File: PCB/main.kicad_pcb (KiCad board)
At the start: 2 copper layers, 64 parts, among them J1 S20B-PADSS-1, J2 S20B-PADSS-1, J3 SWD, SW1 SPST, U1 TPS5430, U2 AMS1117-3.3, U3 MCP2558FD, U4 MCP2558FD, U5 STM32G0B1, Y1 40M

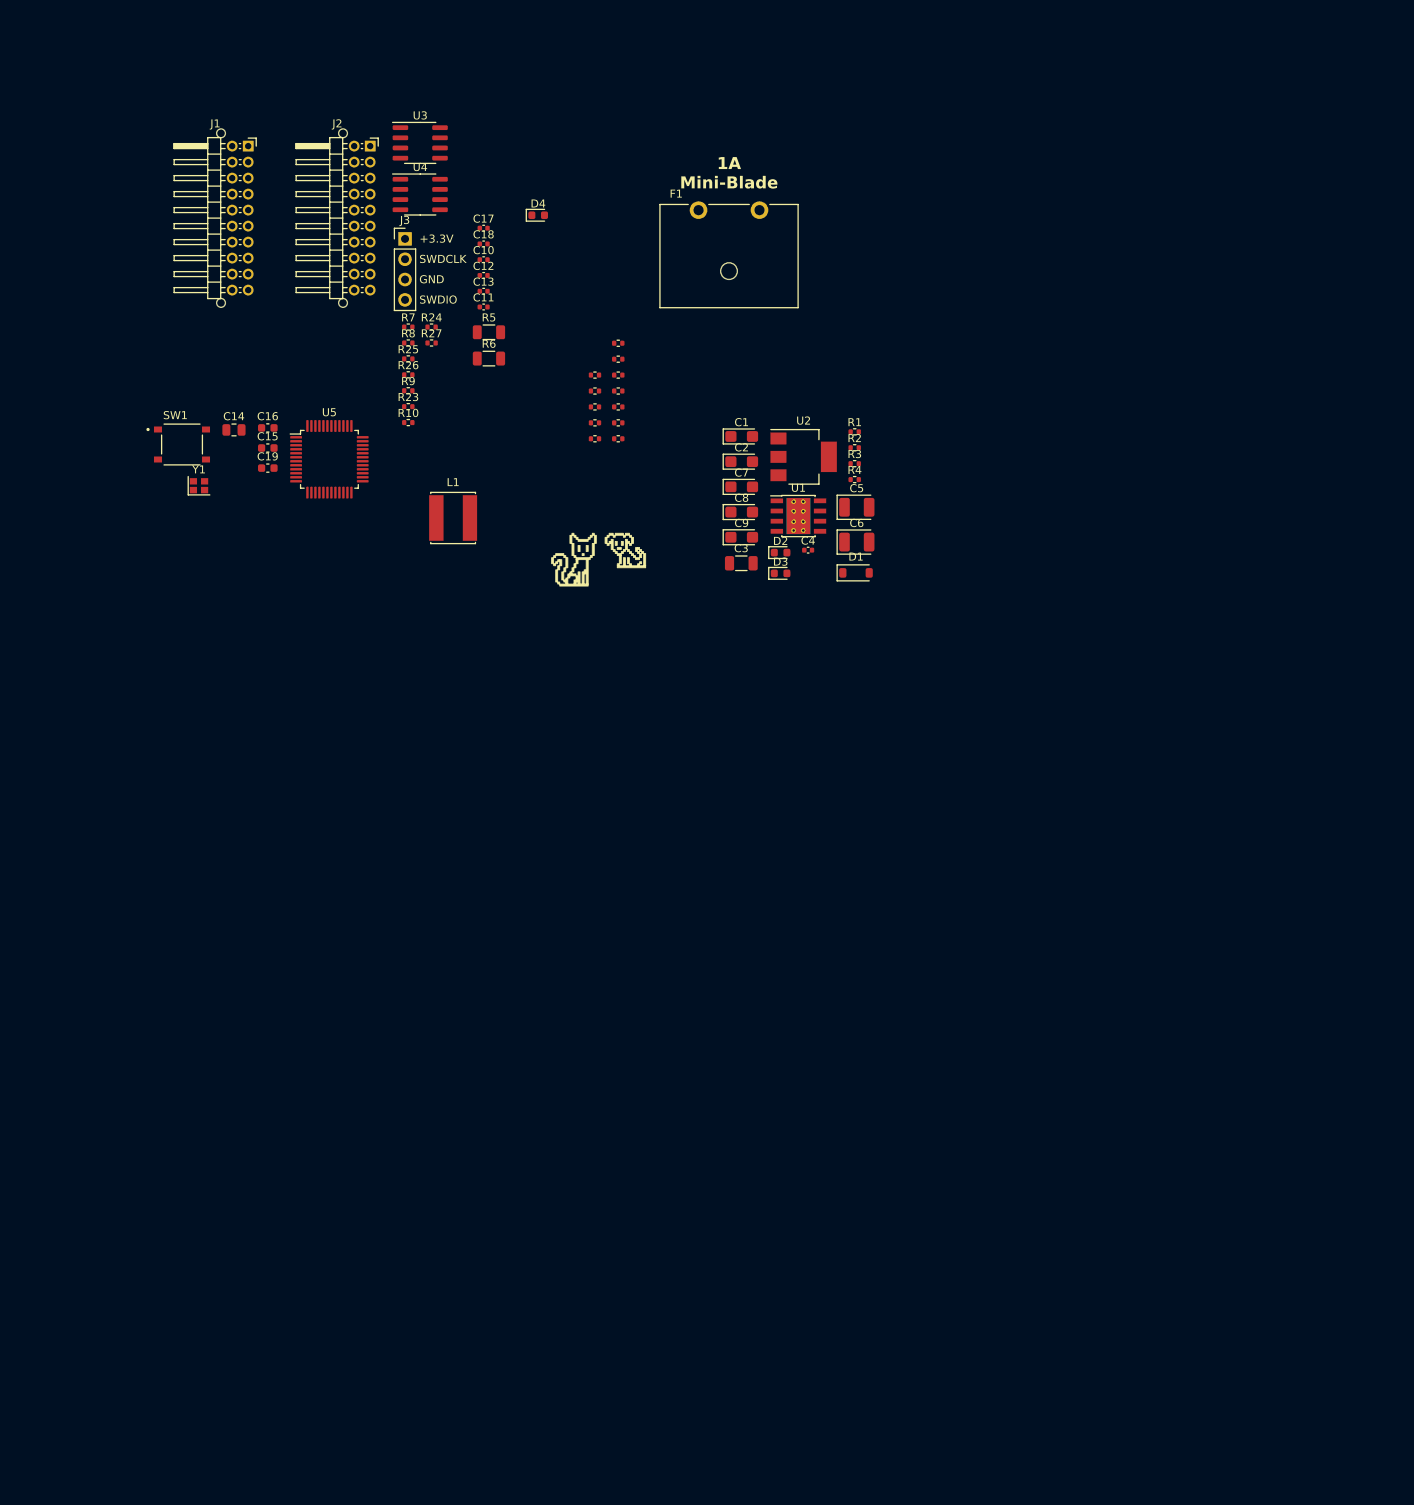
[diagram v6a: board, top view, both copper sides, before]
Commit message: Start layout, but intend to ditch the 0ohm resistors and be confident CAN1 is the right one (remember 0402 links)
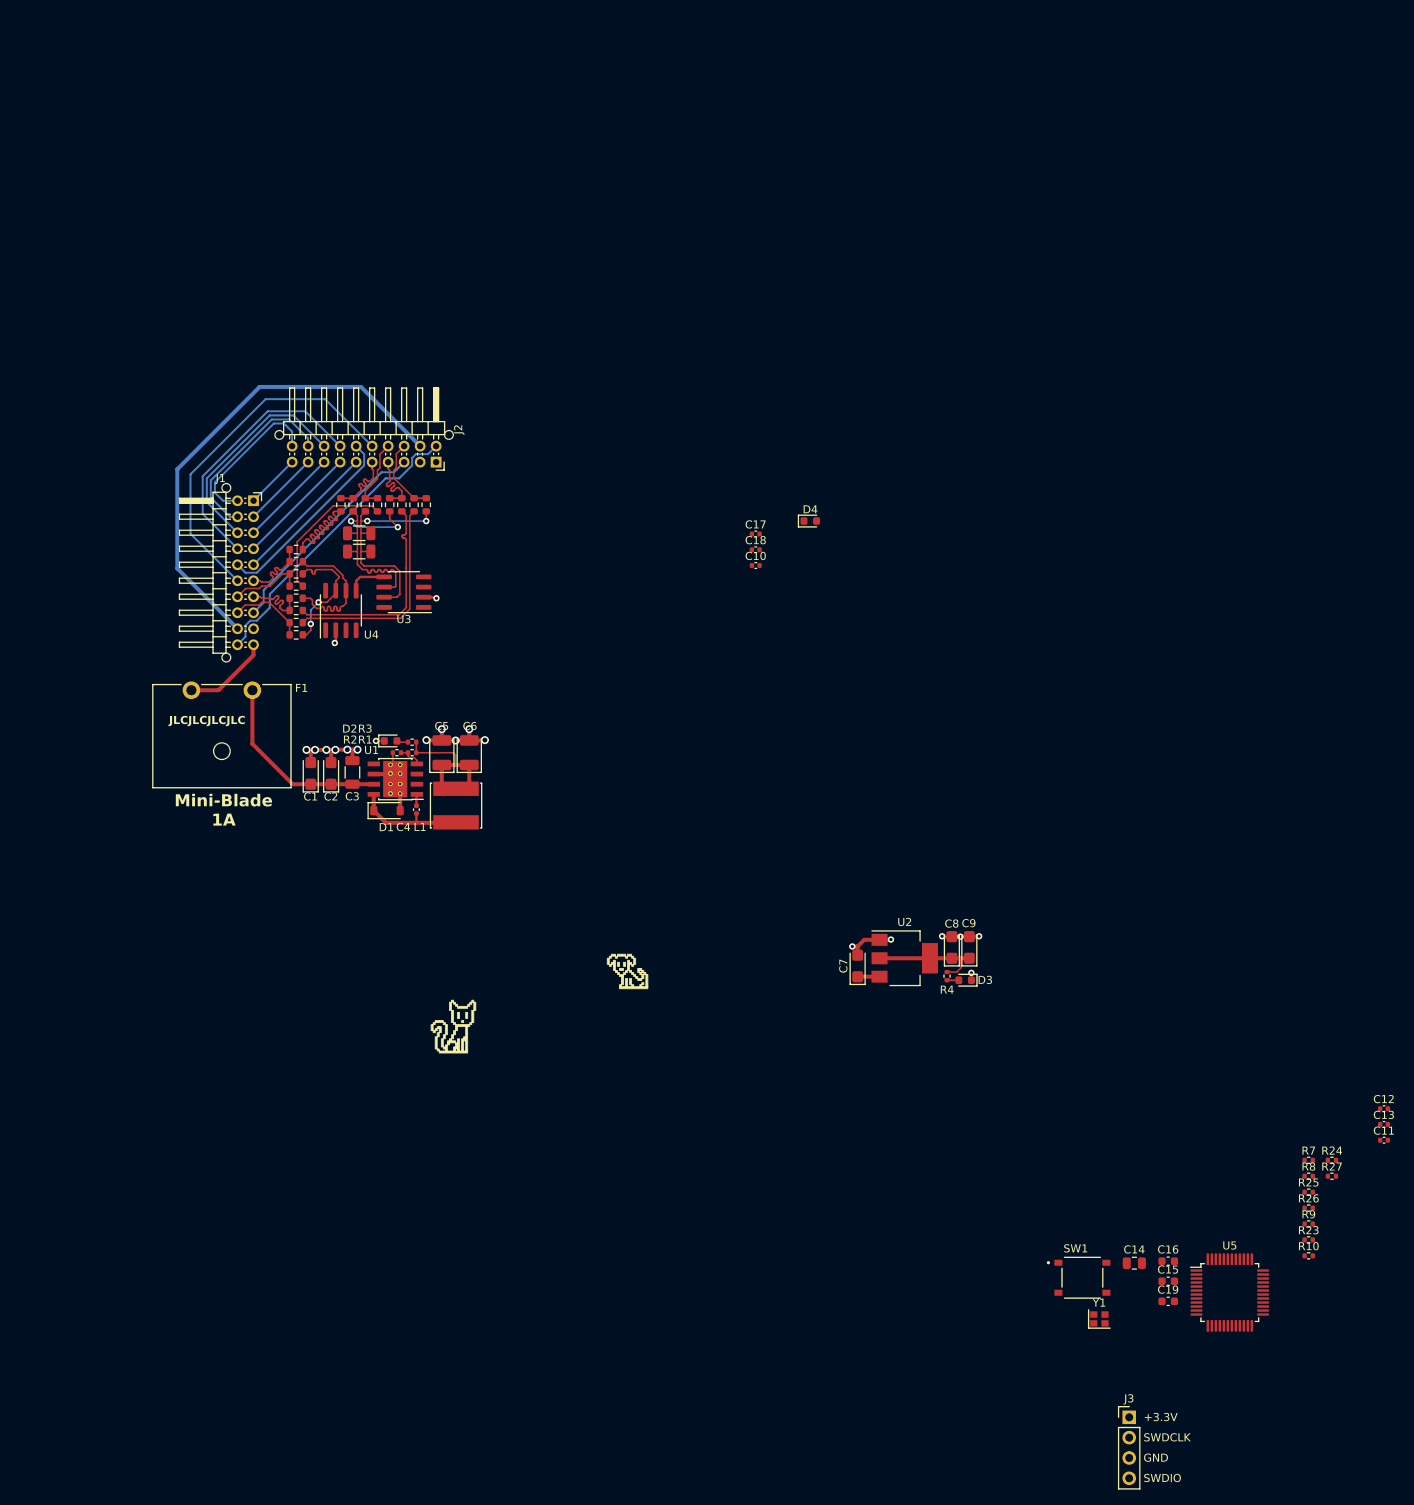
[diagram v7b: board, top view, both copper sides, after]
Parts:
- added ART3: JLCJLCJLCJLC, libdb:CMP-0047, F.Cu at (28.7, 90.0)
- added R28: 0, Resistor_SMD:R_0603_1608Metric, F.Cu at (47.5, 64.8)
- added R29: 0, Resistor_SMD:R_0603_1608Metric, F.Cu at (42.9, 64.8)
- added R30: 0, Resistor_SMD:R_0603_1608Metric, F.Cu at (52.1, 64.8)
- added R31: 0, Resistor_SMD:R_0603_1608Metric, F.Cu at (50.5, 64.8)
- R11, R12, R13, R14, R15, R16, R17, R18, R19, R20, R21, R22: footprint Resistor_SMD:R_0402_1005Metric -> Resistor_SMD:R_0603_1608Metric
- moved J3 172.9 mm to (141.5, 178.8)
- moved C15 153.3 mm to (146.3, 161.8)
- moved C16 153.3 mm to (146.3, 159.3)
- moved C19 153.3 mm to (146.3, 164.3)
- moved R10 153.3 mm to (163.9, 158.6)
- moved R24 153.3 mm to (166.8, 146.7)
- moved R26 153.3 mm to (163.9, 152.7)
- moved R27 153.3 mm to (166.8, 148.7)
- moved R7 153.3 mm to (163.9, 146.7)
- moved R8 153.3 mm to (163.9, 148.7)
- moved R9 153.3 mm to (163.9, 154.7)
- moved SW1 153.3 mm to (135.6, 161.4)
- moved Y1 153.3 mm to (137.7, 166.5)
- moved C11 153.3 mm to (173.3, 144.2)
- moved C12 153.3 mm to (173.3, 140.3)
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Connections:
- net /JST_06_CAN1L renamed /IN_CAN1-
- net /JST_07_CAN2L_NC renamed /IN_NC_CAN2-
- net /JST_17_CAN1H renamed /IN_CAN1+
- net /JST_18_CAN2H_NC renamed /IN_NC_CAN2+
- net /Relay_IN_CANH renamed /Relay_IN_CAN+
- net /Relay_IN_CANL renamed /Relay_IN_CAN-
- net /Relay_OUT_CANH renamed /Relay_OUT_CAN+
- net /Relay_OUT_CANL renamed /Relay_OUT_CAN-
- F1 pad 1: +BATT -> /JST_10_BAT+
- F1 pad 2: /JST_10_BAT+ -> +BATT
- J2 pad 13: /CAN2H_NC -> /NC_CAN2+
- J2 pad 14: /CAN1H -> /CAN1+
- J2 pad 4: /CAN2L_NC -> /NC_CAN2-
- J2 pad 5: /CAN1L -> /CAN1-
- R15 pad 1: /CAN1H -> /CAN1+
- R16 pad 1: /CAN2H_NC -> /NC_CAN2+
- R17 pad 1: /CAN1H -> /CAN1-
- R18 pad 1: /CAN2H_NC -> /NC_CAN2-
- R19 pad 1: /CAN1H -> /FW_CAN1+
- R20 pad 1: /CAN1L -> /FW_CAN1-
- R21 pad 1: /CAN2H_NC -> /FW_NC_CAN2+
- R22 pad 1: /CAN2L_NC -> /FW_NC_CAN2-
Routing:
- net /JST_19_CAM_12V+: track 0.00 -> 60.7 mm
- net /JST_10_BAT+: track 0.00 -> 50.9 mm
- net /JST_16_NC: track 0.00 -> 44.8 mm
- net Earth: track 0.00 -> 42.8 mm, vias 0 -> 20
- net /JST_20_NC: track 0.00 -> 37.5 mm
- net /JST_14_AUDIO_FL: track 0.00 -> 33.2 mm
- net /Relay_OUT_CAN+: track 0.00 -> 28.8 mm, vias 0 -> 2
- net /Relay_OUT_CAN-: track 0.00 -> 28.6 mm, vias 0 -> 2
- net /JST_13_AUDIO_FL: track 0.00 -> 27.9 mm
- net /JST_08_CAM_DET: track 0.00 -> 27.5 mm
- net /FW_NC_CAN2+: track 0.00 -> 26.5 mm
- net /FW_NC_CAN2-: track 0.00 -> 26.5 mm
- net /JST_15_VID_IN: track 0.00 -> 24.6 mm
- net +BATT: track 0.00 -> 24.0 mm
- net /JST_12_AUDIO_FL: track 0.00 -> 23.7 mm
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- added copper zone on In1.Cu, net Earth
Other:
- copper layers 2 -> 4
- board text added: "Mini-Blade 1A"
- board text removed: "1A Mini-Blade"

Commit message: Start relayout
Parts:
- removed R28, R29, R30, R31: 0, Resistor_SMD:R_0603_1608Metric
- R11, R12, R13, R14, R15, R16, R17, R18, R19, R20, R21, R22: footprint Resistor_SMD:R_0603_1608Metric -> Resistor_SMD:R_0402_1005Metric
- U1: footprint Package_SO:TI_SO-PowerPAD-8_ThermalVias -> libdb:CMP-0030
- moved J3 142.3 mm to (105.0, 41.2)
- moved C11 136.1 mm to (71.7, 53.7), turned to -90 degrees
- moved U5 123.7 mm to (119.1, 44.6)
- moved Y1 119.7 mm to (126.7, 47.3)
- moved R23 115.1 mm to (117.8, 51.2)
- moved R10 112.7 mm to (114.9, 57.2)
- moved R9 110.9 mm to (114.9, 55.2)
- moved C15 108.7 mm to (111.3, 58.9)
- moved SW1 108.4 mm to (124.2, 53.6)
- moved R7 107.3 mm to (114.9, 51.2)
- moved R8 107.3 mm to (114.9, 53.2)
- moved C19 106.4 mm to (111.3, 63.9)
- moved R25 106.0 mm to (117.8, 55.2)
- moved R26 106.0 mm to (117.8, 57.2)
- moved R24 105.5 mm to (117.8, 53.2)
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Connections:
- net Earth renamed GND
- net Net-(D1-K) renamed /PH
- F1 pad 1: /JST_10_BAT+ -> +BATT
- F1 pad 2: +BATT -> /JST_10_BAT+
- R12 pad 1: /Relay_IN_CAN+ -> /NC_CAN2+
- R12 pad 2: /IN_NC_CAN2+ -> /FW_CAN2+
- R14 pad 1: /Relay_IN_CAN- -> /NC_CAN2-
- R14 pad 2: /IN_NC_CAN2- -> /FW_CAN2-
- R16 pad 1: /NC_CAN2+ -> /Relay_IN_CAN+
- R16 pad 2: /Relay_OUT_CAN+ -> /N2+
- R18 pad 1: /NC_CAN2- -> /Relay_IN_CAN-
- R18 pad 2: /Relay_OUT_CAN- -> /N2-
- R19 pad 1: /FW_CAN1+ -> /Relay_OUT_CAN+
- R19 pad 2: /IN_CAN1+ -> /N1+
- R20 pad 1: /FW_CAN1- -> /Relay_OUT_CAN-
- R20 pad 2: /IN_CAN1- -> /N1-
- R21 pad 1: /FW_NC_CAN2+ -> /FW_CAN2+
- R22 pad 1: /FW_NC_CAN2- -> /FW_CAN2-
- R5 pad 1: /Relay_OUT_CAN- -> /N1-
- R5 pad 2: /Relay_OUT_CAN+ -> /N1+
- R6 pad 1: /Relay_OUT_CAN- -> /N1-
- R6 pad 2: /Relay_OUT_CAN+ -> /N1+
- U3 pad 6: /Relay_OUT_CAN- -> /N1-
- U3 pad 7: /Relay_OUT_CAN+ -> /N1+
- U4 pad 6: /Relay_IN_CAN- -> /N2-
- U4 pad 7: /Relay_IN_CAN+ -> /N2+
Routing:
- net /JST_10_BAT+: track 50.9 -> 0.00 mm
- net /FW_CAN2-: track 0.00 -> 37.8 mm, vias 0 -> 2
- net /FW_CAN2+: track 0.00 -> 37.8 mm, vias 0 -> 2
- net /JST_01_AUX_IN: track 6.82 -> 44.6 mm
- net /JST_02_AUX_IN: track 9.65 -> 43.3 mm
- net GND: track 42.8 -> 9.86 mm, vias 20 -> 16
- net /JST_03_AUX_IN: track 12.5 -> 44.6 mm
- net /JST_11_AUDIO_FL: track 19.5 -> 48.8 mm
- net /JST_04_NC: track 15.3 -> 43.3 mm
- net /JST_12_AUDIO_FL: track 23.7 -> 51.4 mm
- net /Relay_OUT_CAN+: track 28.8 -> 1.30 mm, vias 2 -> 0
- net /Relay_OUT_CAN-: track 28.6 -> 1.30 mm, vias 2 -> 0
- net /FW_NC_CAN2+: track 26.5 -> 0.00 mm
- net /FW_NC_CAN2-: track 26.5 -> 0.00 mm
- net /JST_05_BK_VID_IN: track 18.1 -> 43.8 mm
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- added copper zone on F.Cu, net +3.3V
- added copper zone on F.Cu, net +5V
- added copper zone on F.Cu, net +BATT
- added copper zone on In2.Cu, net /JST_10_BAT+
- added copper zone on F.Cu, net /PH
- added copper zone on F.Cu, net GND
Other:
- board outline added: 115.2 x 62.3 mm
- board text added: "1A Mini-Blade"
- board text removed: "Mini-Blade 1A"
